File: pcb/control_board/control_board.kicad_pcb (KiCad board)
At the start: 2 copper layers, 152.4 x 95.2 mm, 49 parts, among them J1 Barrel_Jack, J2 Conn_01x24_Female, J3 Conn_01x24_Female, J4 Conn_02x06_Top_Bottom, SW1 SW_Push, SW2 SW_Push, SW3 SW_Push, SW4 SW_Push, SW5 SW_Push, SW6 SW_Push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

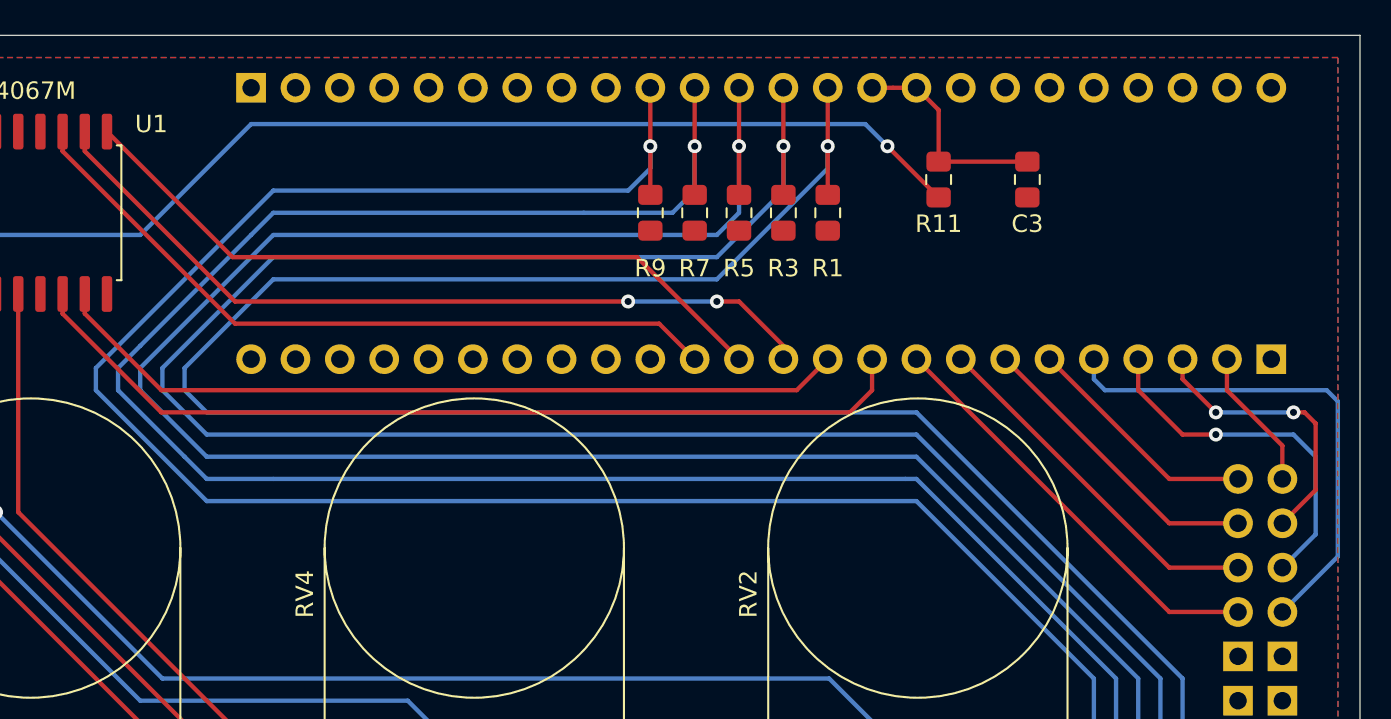
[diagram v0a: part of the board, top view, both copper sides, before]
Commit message: Correctly place CMOD headers, add divider to filter to drop potentiometer voltage into range of CMOD ADC.
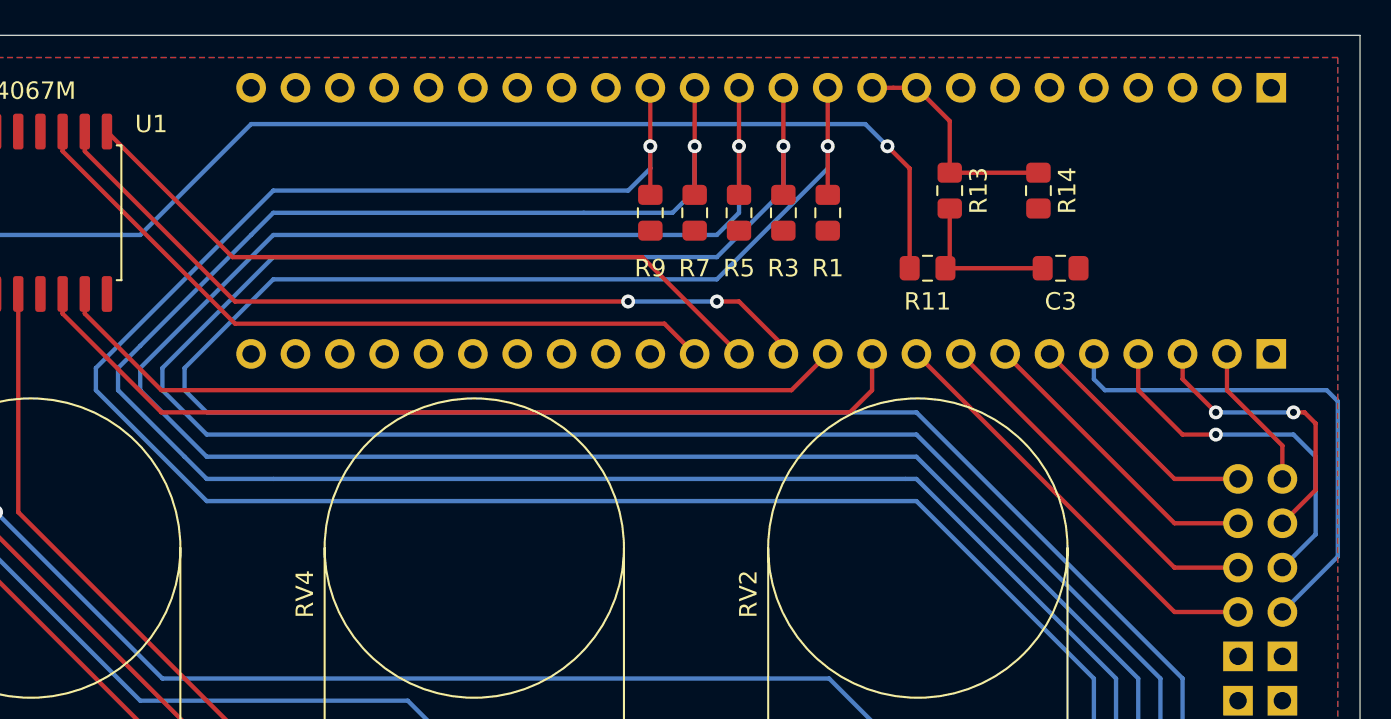
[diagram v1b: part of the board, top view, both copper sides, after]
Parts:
- added R13: 10k, Resistor_SMD:R_0805_2012Metric_Pad1.15x1.40mm_HandSolder, F.Cu at (202.6, 50.8)
- added R14: 38k, Resistor_SMD:R_0805_2012Metric_Pad1.15x1.40mm_HandSolder, F.Cu at (207.6, 50.8)
- moved J2 58.4 mm to (221.0, 44.9), turned to 90 degrees
- moved C3 5.43 mm to (208.9, 55.2), turned to 0 degrees
- moved R11 5.12 mm to (201.3, 55.2), turned to 0 degrees
- moved J3 0.30 mm to (221.0, 60.2)
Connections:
- C3 pad 1: AN_FILT -> Net-(C3-Pad1)
- R11 pad 2: AN_FILT -> Net-(C3-Pad1)
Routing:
- net Net-(C3-Pad1): track 0.00 -> 9.09 mm
- net AN_RAW: track 68.6 -> 72.0 mm
- net AN_FILT: track 12.4 -> 13.3 mm
- net Net-(J3-Pad12): track 46.5 -> 45.7 mm

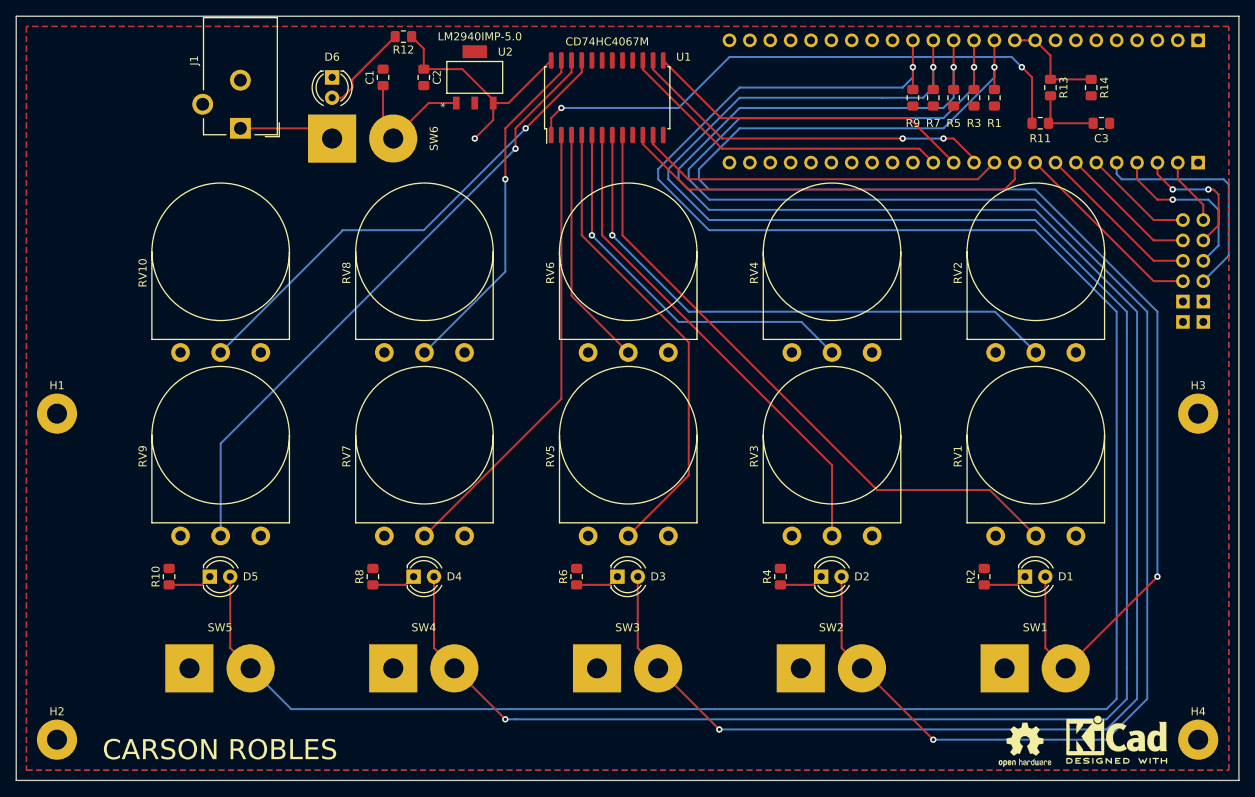
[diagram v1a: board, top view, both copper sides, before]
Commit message: Add connectors for switches rather than holes for direct wires.
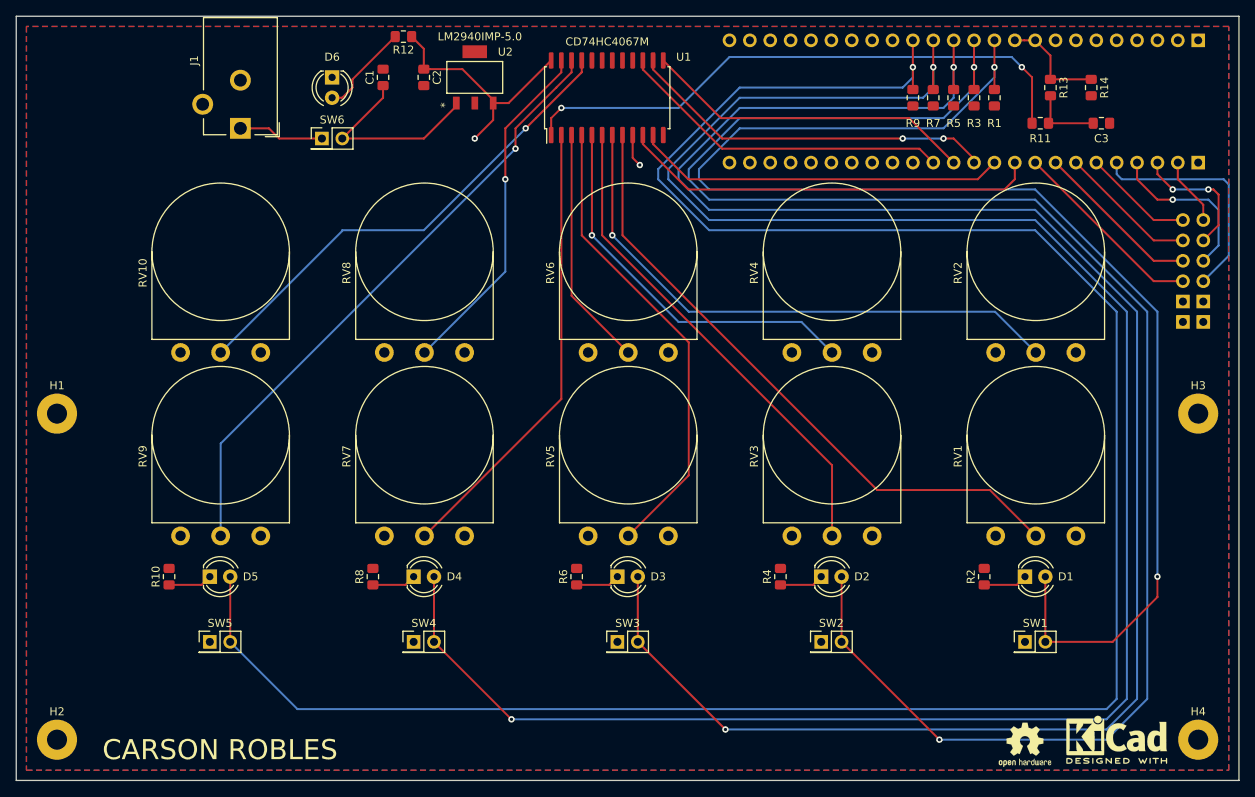
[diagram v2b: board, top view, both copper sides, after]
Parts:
- SW1, SW2, SW3, SW4, SW5, SW6: footprint Connector_Wire:SolderWirePad_1x02_P7.62mm_Drill2.5mm -> Connector_PinHeader_2.54mm:PinHeader_2x01_P2.54mm_Vertical
- moved SW2 4.17 mm to (174.0, 119.9)
- moved SW5 4.17 mm to (97.8, 119.9)
- moved SW1 4.17 mm to (199.4, 119.9)
- moved SW3 4.17 mm to (148.6, 119.9)
- moved SW4 4.17 mm to (123.2, 119.9)
- moved SW6 1.27 mm to (111.8, 57.1)
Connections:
- U1 pad 9: Net-(U1-Pad9) -> 5V
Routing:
- net Net-(C1-Pad1): track 16.8 -> 25.0 mm
- net 5V: track 30.1 -> 34.2 mm, vias 1 -> 2
- net distortion_en: track 175.9 -> 174.2 mm
- net VCC: track 12.0 -> 10.7 mm
